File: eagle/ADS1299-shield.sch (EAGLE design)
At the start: 124 parts, among them CN1 External Clock, IC1 ADS1299IPAG, IC2 TPS72325DBVT, IC3 TPS73225DBVT, IC5 24AA256UID, IC6 TPS604XXDBV, IC7 OPA376DBV, IC8 OPA376DBV, J8 Electrode Connector, U2 TXB0108PWR, U3 TXB0108PWR

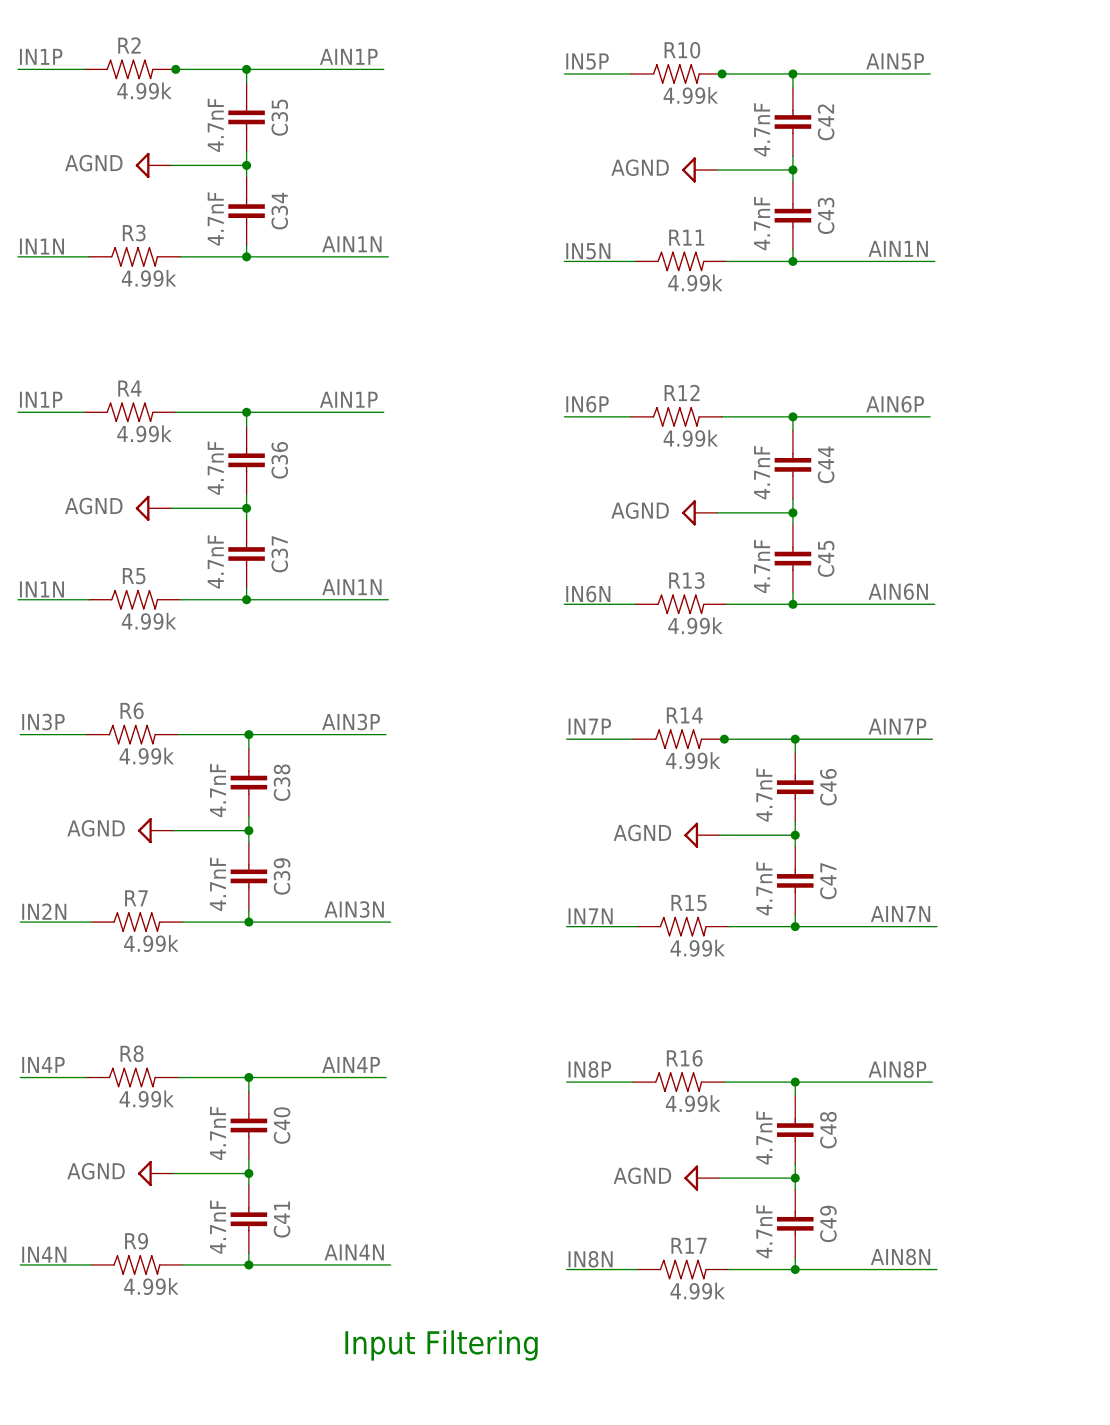
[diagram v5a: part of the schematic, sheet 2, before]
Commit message: arranged components by function - AIN filters, ADC and decoupling, power, SRB, Bias, level shifters, EEPROM
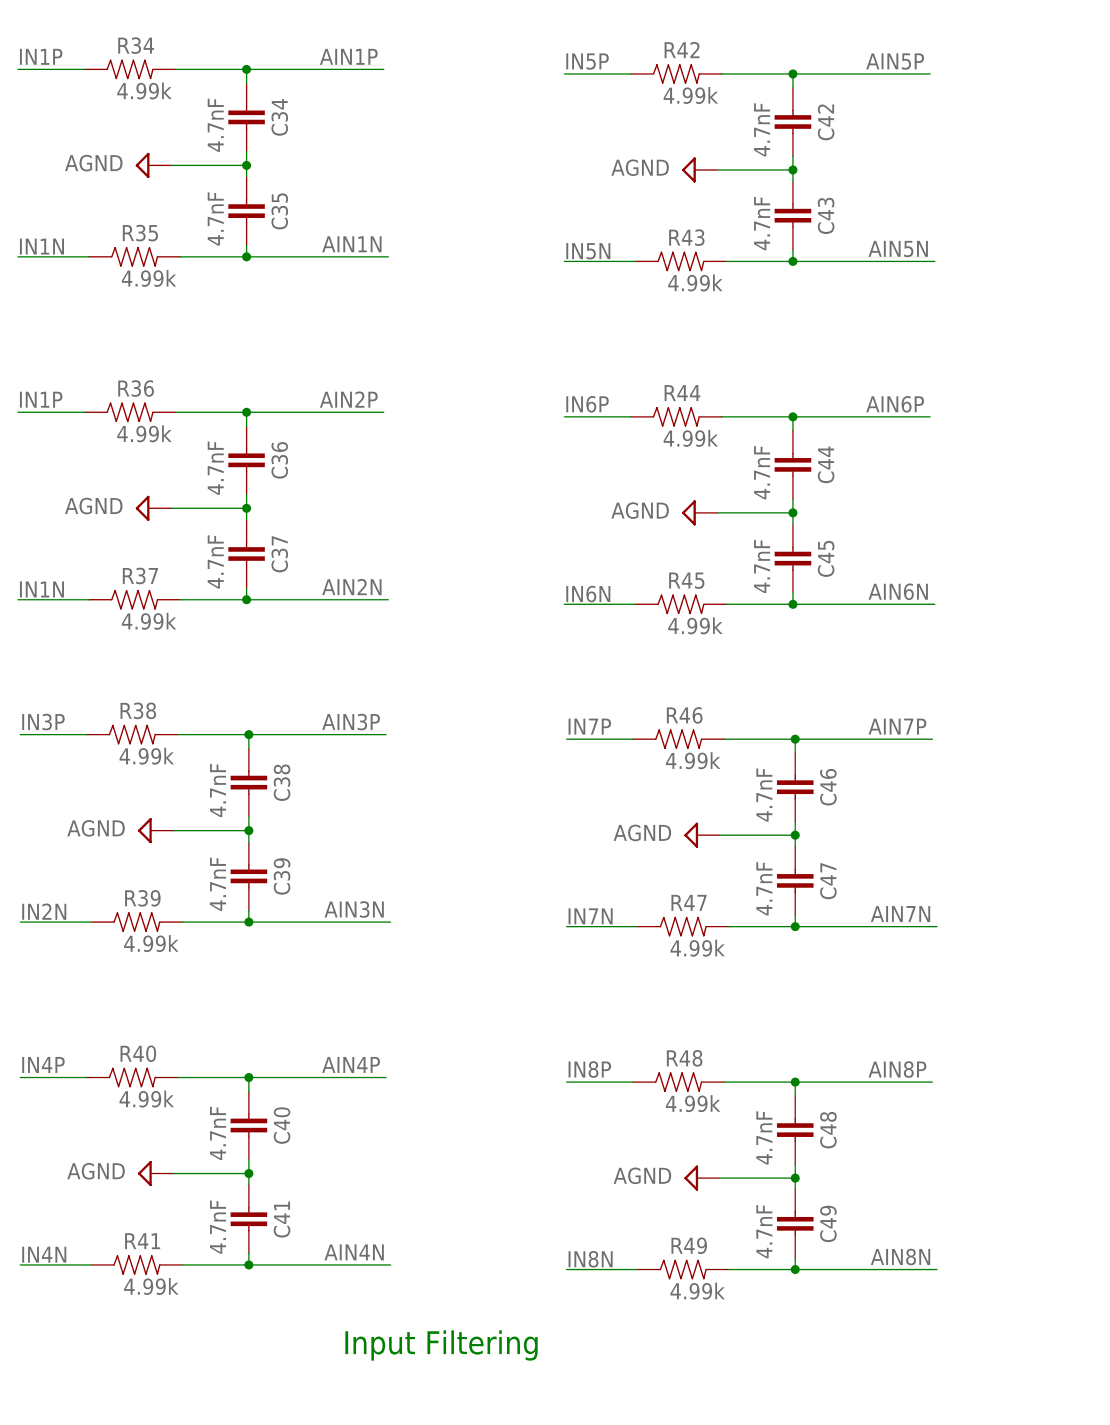
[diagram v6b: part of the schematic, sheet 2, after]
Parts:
- added U$2: FIDUCIAL, adafruit:FIDUCIAL
- renumbered R10 to R42, R11 to R43, R12 to R44, R13 to R45, R14 to R46, R15 to R47, R16 to R48, R17 to R49, R2 to R34, R3 to R35, R4 to R36, R5 to R37, R6 to R38, R7 to R39, R8 to R40, R9 to R41
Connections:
- net AGND: now also C34.2, C35.1; no longer C34.1, C35.2
- net AIN1N: now also C35.2; no longer C34.2, C37.2, C43.2, R37.2, R43.2
- net AIN1P: now also C34.1; no longer C35.1, C36.1, R36.2
- net AIN2N: now also C37.2, R37.2
- net AIN2P: now also C36.1, R36.2
- net AIN5N: now also C43.2, R43.2
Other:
- moved on the sheet: C34, C35

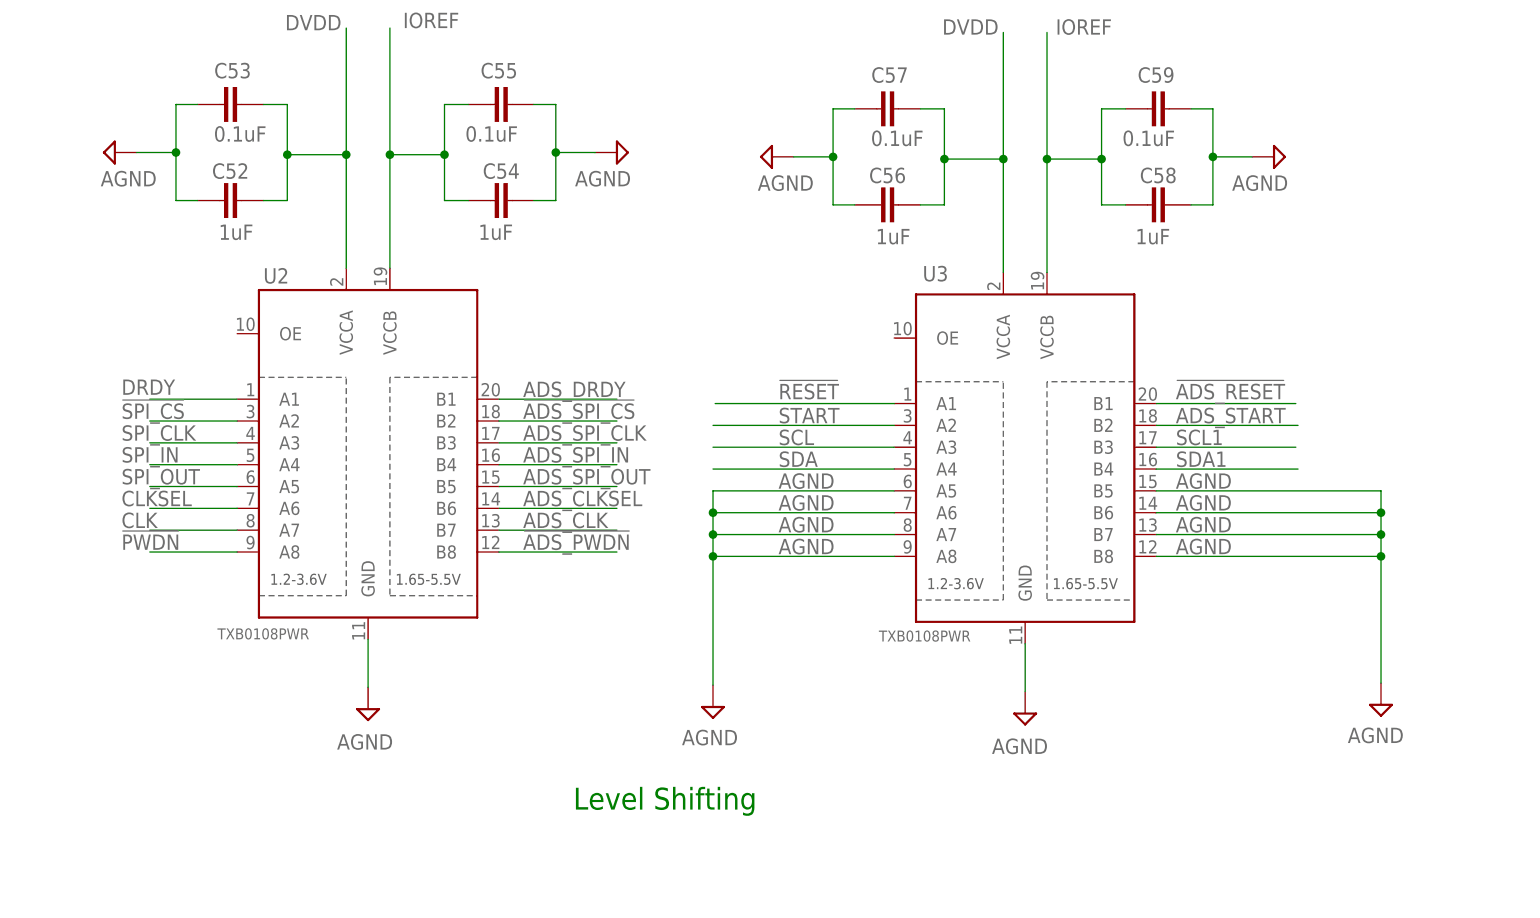
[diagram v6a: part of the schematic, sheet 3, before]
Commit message: fixed errors in AIN block; some airwires; level shifter output enable is now connected and held high
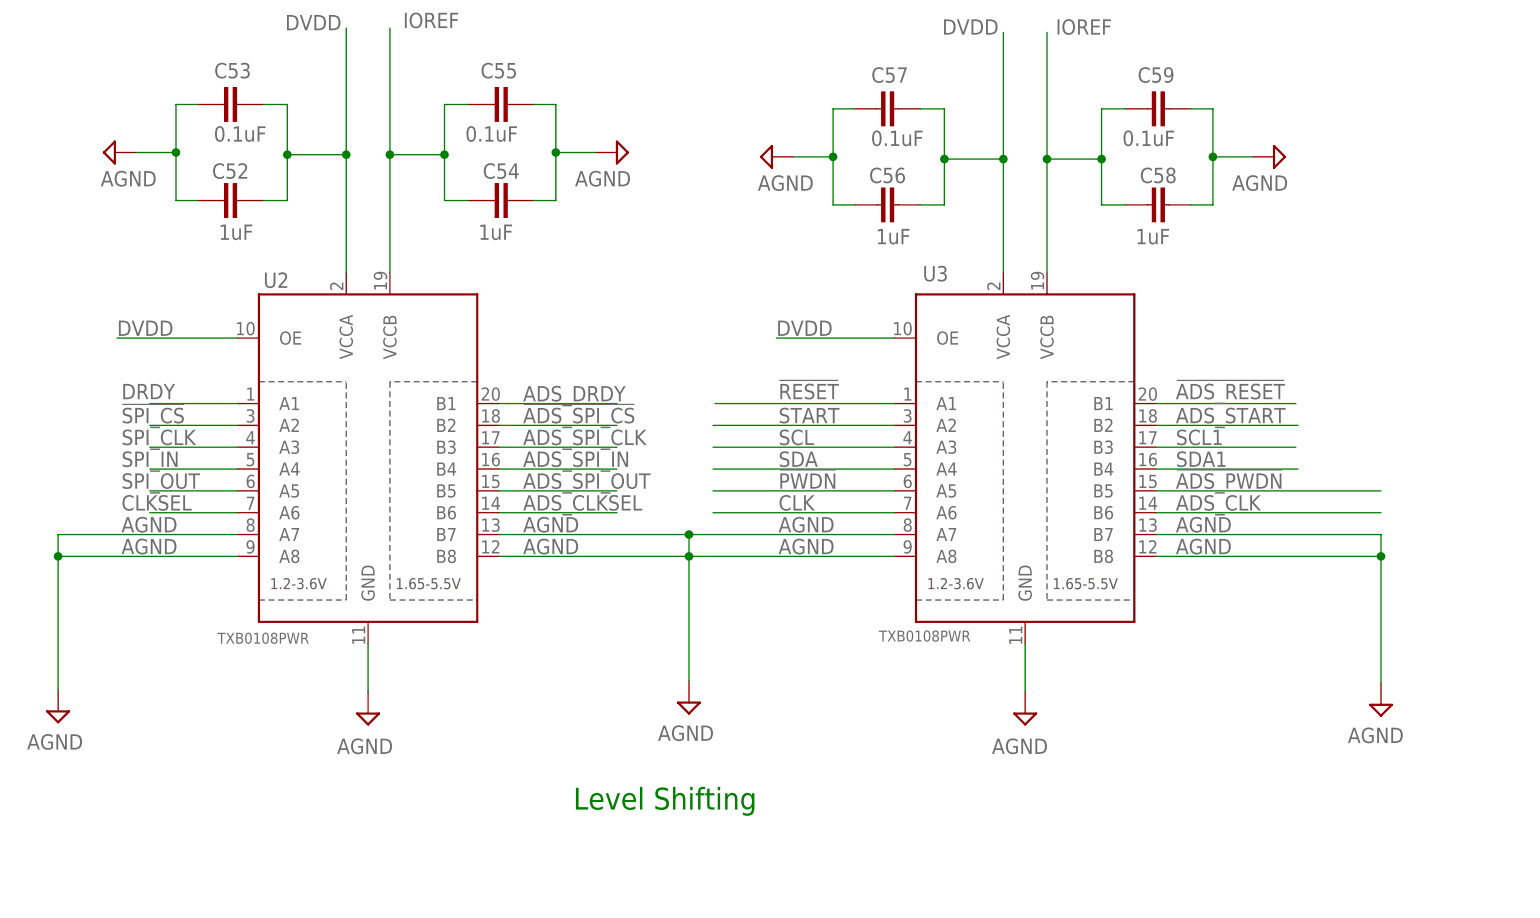
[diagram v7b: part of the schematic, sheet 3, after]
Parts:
- renumbered JP16 to TP1, JP18 to TP2
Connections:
- net !ADS_PWDN: now also U3.B5; no longer U2.B8
- net !PWDN: now also U3.A5; no longer U2.A8
- net ADS_CLK: now also U3.B6; no longer U2.B7
- net AGND: now also U2.A7, U2.A8, U2.B7, U2.B8; no longer U3.A5, U3.A6, U3.B5, U3.B6
- net CLK: now also U3.A6; no longer U2.A7
- net DVDD: now also U2.OE, U3.OE
- net IN1N: no longer R37.1
- net IN1P: no longer R36.1
- net IN2N: now also R37.1; no longer R39.1
- net IN2P: now also R36.1
- net IN3N: now also R39.1
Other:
- moved on the sheet: U2

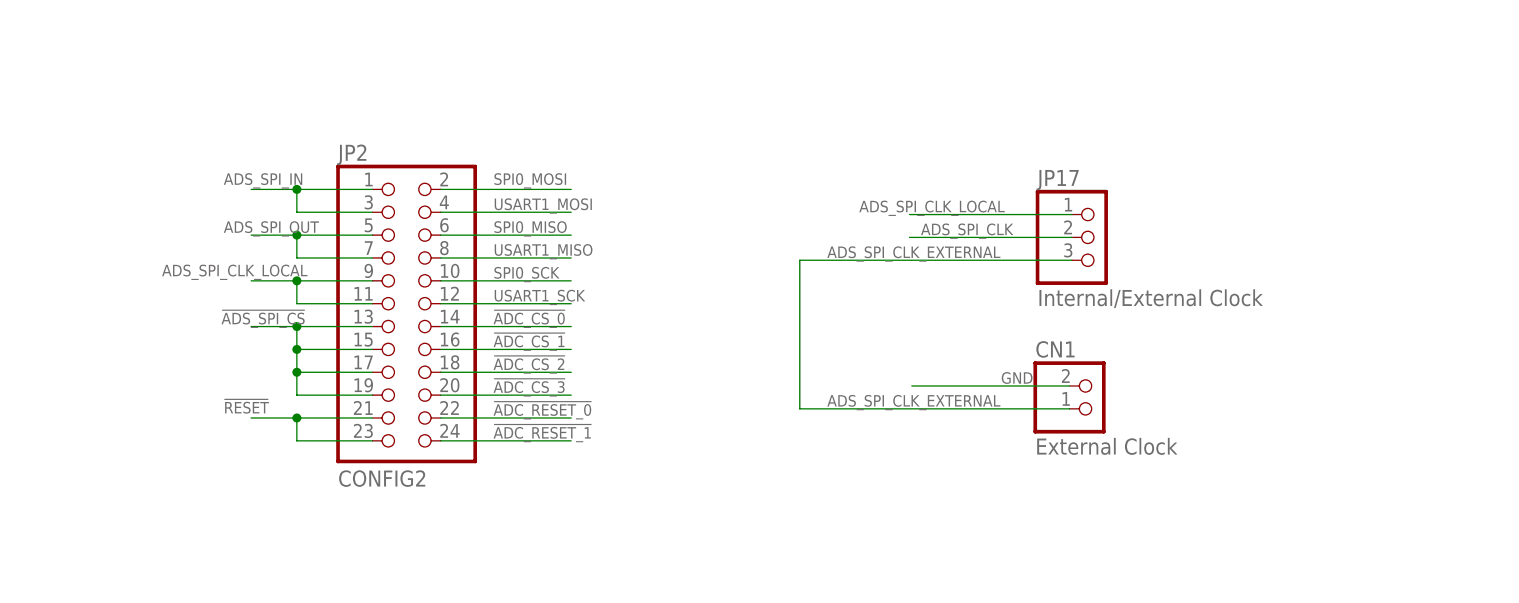
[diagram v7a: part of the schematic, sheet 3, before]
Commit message: changed sync connector to jst 3-pin to support start and clock signals; moved components to place jst connector at board left edge; made ground and power polygons
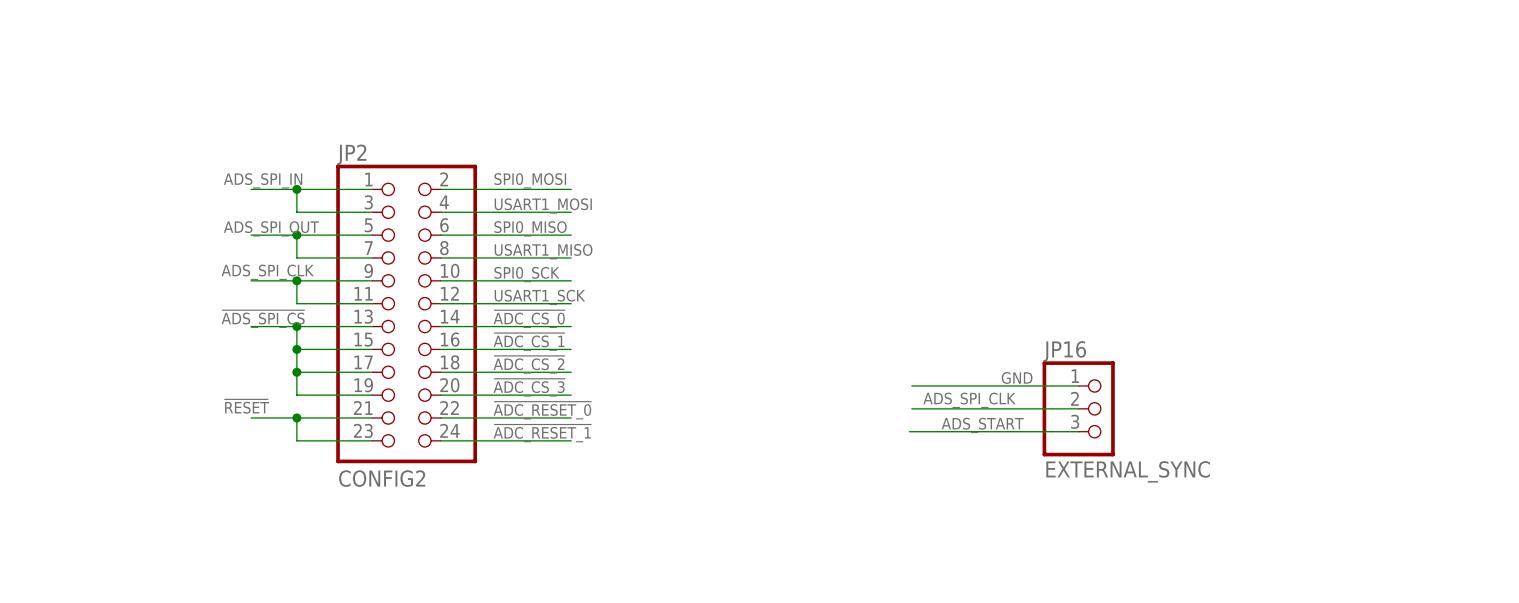
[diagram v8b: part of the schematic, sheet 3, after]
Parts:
- removed CN1: External Clock, adafruit:JST_2PIN-SMT-RA
- removed JP17: Internal/External Clock, adafruit:PINHD-1X3
- added JP16: EXTERNAL_SYNC, adafruit:JST_3PIN
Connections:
- removed net ADS_SPI_CLK_EXTERNAL: CN1.2, JP17.3
- removed net ADS_SPI_CLK_LOCAL: JP17.1, JP2.11, JP2.9
- net ADS_SPI_CLK: now also JP16.2, JP2.11, JP2.9; no longer JP17.2
- net ADS_START: now also JP16.3
- net GND: now also JP16.1; no longer CN1.1
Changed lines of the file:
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@@
 <part name="JP14" library="SmartPrj" deviceset="PINHD-1X8" device="" value="POWER"/>
 <part name="JP15" library="SmartPrj" deviceset="PINHD-2X3" device="" value="SPI"/>
-<part name="JP17" library="adafruit" deviceset="PINHD-1X3" device="" value="Internal/External Clock"/>
-<part name="CN1" library="adafruit" deviceset="JST_2PIN" device="-SMT-RA" value="External Clock"/>
 <part name="TP1" library="adafruit" deviceset="PINHD-1X1" device="" value="AVDD_TEST_POINT"/>
 <part name="TP2" library="adafruit" deviceset="PINHD-1X1" device="" value="AVSS_TEST_POINT"/>
@@
 <part name="R34" library="SparkFun-Passives" deviceset="RESISTOR" device="0603-RES" value="4.99k"/>
 <part name="SUPPLY51" library="supply2" deviceset="AGND" device=""/>
+<part name="JP16" library="adafruit" deviceset="JST_3PIN" device="" value="EXTERNAL_SYNC"/>
 </parts>
 <sheets>
@@
 <instance part="JP14" gate="A" x="304.8" y="240.03"/>
 <instance part="JP15" gate="A" x="335.28" y="208.28" rot="R270"/>
-<instance part="JP17" gate="A" x="274.574" y="52.07"/>
-<instance part="CN1" gate="G$1" x="274.32" y="33.02"/>
 <instance part="U$5" gate="G$1" x="226.06" y="134.62"/>
 <instance part="U$6" gate="G$1" x="236.22" y="134.62"/>
@@
 <attribute name="VALUE" x="43.053" y="176.911" size="1.778" layer="96" rot="R180"/>
 </instance>
+<instance part="JP16" gate="G$1" x="275.336" y="33.02"/>
 </instances>
 <busses>
@@
 </segment>
 <segment>
-<pinref part="JP17" gate="A" pin="2"/>
-<wire x1="272.034" y1="52.07" x2="254" y2="52.07" width="0.1524" layer="91"/>
-<label x="255.27" y="52.324" size="1.27" layer="95"/>
+<pinref part="JP2" gate="A" pin="9"/>
+<wire x1="194.31" y1="47.244" x2="185.928" y2="47.244" width="0.1524" layer="91"/>
+<pinref part="JP2" gate="A" pin="11"/>
+<wire x1="194.31" y1="44.704" x2="185.928" y2="44.704" width="0.1524" layer="91"/>
+<wire x1="185.928" y1="47.244" x2="185.928" y2="44.704" width="0.1524" layer="91"/>
+<wire x1="185.928" y1="47.244" x2="180.848" y2="47.244" width="0.1524" layer="91"/>
+<junction x="185.928" y="47.244"/>
+<label x="177.546" y="47.752" size="1.27" layer="95"/>
+</segment>
+<segment>
+<wire x1="272.796" y1="33.02" x2="254.254" y2="33.02" width="0.1524" layer="91"/>
+<label x="255.524" y="33.528" size="1.27" layer="95"/>
+<pinref part="JP16" gate="G$1" pin="2"/>
 </segment>
 </net>
@@
 <label x="106.172" y="41.402" size="1.27" layer="95"/>
 </segment>
+<segment>
+<pinref part="JP16" gate="G$1" pin="3"/>
+<wire x1="272.796" y1="30.48" x2="254" y2="30.48" width="0.1524" layer="91"/>
+<label x="257.556" y="30.734" size="1.27" layer="95"/>
+</segment>
 </net>
 <net name="!RESET" class="0">
@@
 </segment>
 </net>
-<net name="ADS_SPI_CLK_LOCAL" class="0">
-<segment>
-<pinref part="JP17" gate="A" pin="1"/>
-<wire x1="272.034" y1="54.61" x2="254" y2="54.61" width="0.1524" layer="91"/>
-<label x="248.412" y="54.864" size="1.27" layer="95"/>
-</segment>
-<segment>
-<pinref part="JP2" gate="A" pin="9"/>
-<wire x1="194.31" y1="47.244" x2="185.928" y2="47.244" width="0.1524" layer="91"/>
-<pinref part="JP2" gate="A" pin="11"/>
-<wire x1="194.31" y1="44.704" x2="185.928" y2="44.704" width="0.1524" layer="91"/>
-<wire x1="185.928" y1="47.244" x2="185.928" y2="44.704" width="0.1524" layer="91"/>
-<wire x1="185.928" y1="47.244" x2="180.848" y2="47.244" width="0.1524" layer="91"/>
-<junction x="185.928" y="47.244"/>
-<label x="170.942" y="47.752" size="1.27" layer="95"/>
-</segment>
-</net>
-<net name="ADS_SPI_CLK_EXTERNAL" class="0">
-<segment>
-<pinref part="JP17" gate="A" pin="3"/>
-<wire x1="272.034" y1="49.53" x2="241.808" y2="49.53" width="0.1524" layer="91"/>
-<label x="244.856" y="49.784" size="1.27" layer="95"/>
-<wire x1="241.808" y1="49.53" x2="241.808" y2="33.02" width="0.1524" layer="91"/>
-<pinref part="CN1" gate="G$1" pin="2"/>
-<wire x1="271.78" y1="33.02" x2="241.808" y2="33.02" width="0.1524" layer="91"/>
-<label x="244.856" y="33.274" size="1.27" layer="95"/>
-</segment>
-</net>
 <net name="GND" class="0">
 <segment>
-<pinref part="CN1" gate="G$1" pin="1"/>
-<wire x1="271.78" y1="35.56" x2="254.254" y2="35.56" width="0.1524" layer="91"/>
+<wire x1="272.796" y1="35.56" x2="254.254" y2="35.56" width="0.1524" layer="91"/>
 <label x="264.16" y="35.814" size="1.27" layer="95"/>
+<pinref part="JP16" gate="G$1" pin="1"/>
 </segment>
 </net>
